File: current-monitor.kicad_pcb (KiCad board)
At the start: 2 copper layers, 50 x 50 mm, 60 parts, among them J1 SENSE, J2 BATTERY, J3 LCD5110, J4 UART, J5 SWD, J6 JTAG, Q1 MUN5314DW1, U1 AP2210K-3.3, U2 MKL03Z8VFK4, U3 MCP6V71U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

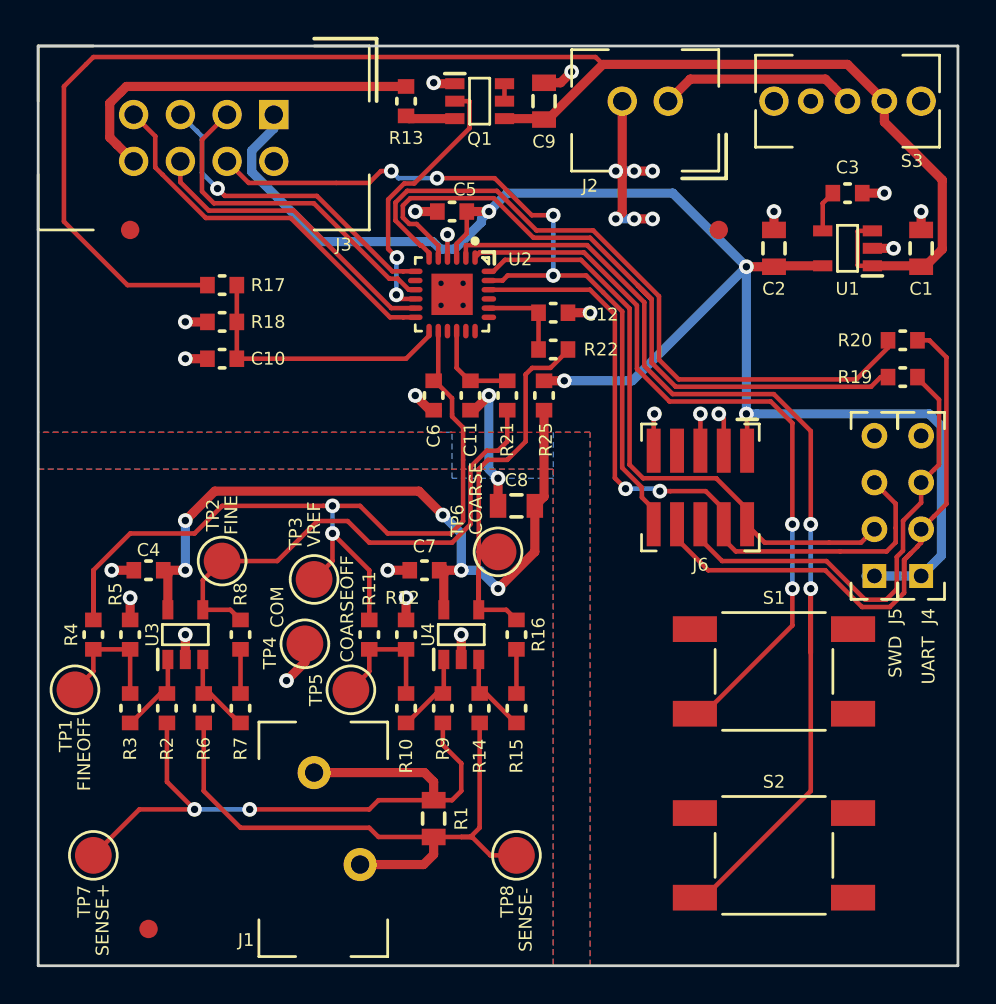
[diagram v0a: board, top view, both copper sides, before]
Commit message: improve power routing
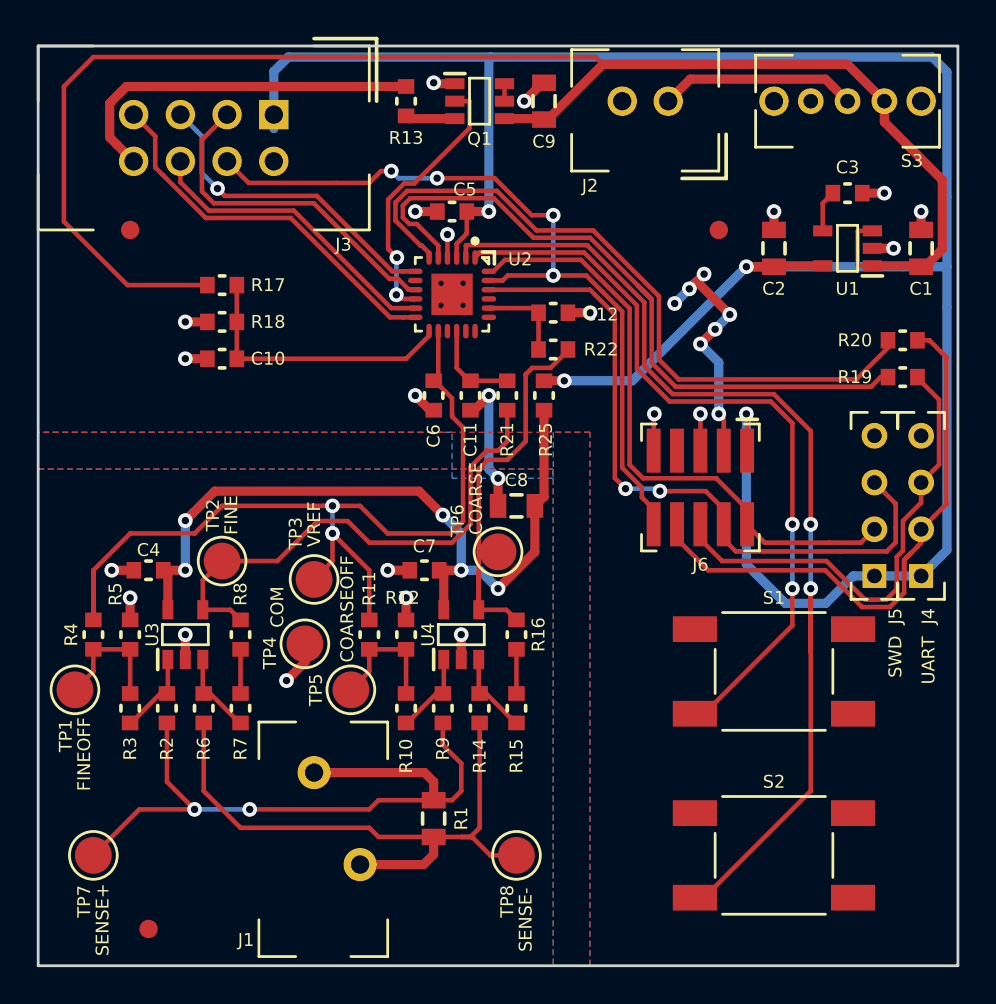
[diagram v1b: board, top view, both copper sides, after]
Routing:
- net +3V3: track 89.4 -> 131.0 mm
- net COM: track 49.6 -> 51.2 mm
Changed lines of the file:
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@@
     (thickness 1.6)
     (drawings 6)
-    (tracks 517)
+    (tracks 519)
     (zones 0)
     (modules 60)
@@
   (segment (start 125 112.8) (end 123 112.8) (width 0.25) (layer F.Cu) (net 3))
   (segment (start 125 112.8) (end 125 115.2) (width 0.25) (layer F.Cu) (net 3))
-  (segment (start 137.4 86.8) (end 138.4 86.8) (width 0.5) (layer F.Cu) (net 4))
-  (via (at 138.4 86.8) (size 0.8) (drill 0.4) (layers F.Cu B.Cu) (net 4))
-  (segment (start 136.4 86.8) (end 137.4 86.8) (width 0.5) (layer B.Cu) (net 4))
-  (via (at 137.4 86.8) (size 0.8) (drill 0.4) (layers F.Cu B.Cu) (net 4))
-  (segment (start 136.75 87) (end 136.6 87) (width 0.5) (layer F.Cu) (net 4))
-  (segment (start 136.6 87) (end 136.4 86.8) (width 0.5) (layer F.Cu) (net 4))
-  (via (at 136.4 86.8) (size 0.8) (drill 0.4) (layers F.Cu B.Cu) (net 4))
-  (segment (start 136.75 87) (end 136.75 89.05) (width 0.5) (layer F.Cu) (net 4))
-  (segment (start 136.75 83) (end 136.75 87) (width 0.5) (layer F.Cu) (net 4))
-  (segment (start 136.75 87) (end 136.75 86.8) (width 0.5) (layer F.Cu) (net 4))
-  (segment (start 137.4 89.4) (end 138.4 89.4) (width 0.5) (layer F.Cu) (net 4))
-  (via (at 138.4 89.4) (size 0.8) (drill 0.4) (layers F.Cu B.Cu) (net 4))
-  (segment (start 136.4 89.4) (end 137.4 89.4) (width 0.5) (layer B.Cu) (net 4))
-  (via (at 137.4 89.4) (size 0.8) (drill 0.4) (layers F.Cu B.Cu) (net 4))
-  (segment (start 136.75 89.05) (end 136.4 89.4) (width 0.5) (layer F.Cu) (net 4))
-  (via (at 136.4 89.4) (size 0.8) (drill 0.4) (layers F.Cu B.Cu) (net 4))
-  (segment (start 132.5 82) (end 133.4 82) (width 0.5) (layer F.Cu) (net 4))
-  (segment (start 133.4 82) (end 134 81.4) (width 0.5) (layer F.Cu) (net 4))
-  (via (at 134 81.4) (size 0.8) (drill 0.4) (layers F.Cu B.Cu) (net 4))
+  (segment (start 132.5 82) (end 132.425002 82) (width 0.5) (layer F.Cu) (net 4))
+  (segment (start 132.425002 82) (end 131.425002 83) (width 0.5) (layer F.Cu) (net 4))
+  (via (at 131.425002 83) (size 0.8) (drill 0.4) (layers F.Cu B.Cu) (net 4))
+  (segment (start 140.4 93.2) (end 141.2 92.4) (width 0.5) (layer F.Cu) (net 4))
+  (via (at 141.2 92.4) (size 0.8) (drill 0.4) (layers F.Cu B.Cu) (net 4))
+  (segment (start 140.8 92.8) (end 140.4 93.2) (width 0.5) (layer F.Cu) (net 4))
+  (segment (start 140.8 92.8) (end 140.4 93.2) (width 0.5) (layer B.Cu) (net 4))
+  (via (at 140.4 93.2) (size 0.8) (drill 0.4) (layers F.Cu B.Cu) (net 4))
+  (segment (start 142.6 94.6) (end 140.8 92.8) (width 0.5) (layer F.Cu) (net 4))
+  (segment (start 139.6 94) (end 140.8 92.8) (width 0.5) (layer B.Cu) (net 4))
+  (via (at 139.6 94) (size 0.8) (drill 0.4) (layers F.Cu B.Cu) (net 4))
+  (segment (start 141.8 95.4) (end 142.6 94.6) (width 0.5) (layer B.Cu) (net 4))
+  (via (at 142.6 94.6) (size 0.8) (drill 0.4) (layers F.Cu B.Cu) (net 4))
+  (segment (start 141 96.2) (end 141.8 95.4) (width 0.5) (layer F.Cu) (net 4))
+  (via (at 141.8 95.4) (size 0.8) (drill 0.4) (layers F.Cu B.Cu) (net 4))
+  (segment (start 142 100) (end 142 97.2) (width 0.5) (layer B.Cu) (net 4))
+  (segment (start 142 97.2) (end 141 96.2) (width 0.5) (layer B.Cu) (net 4))
+  (via (at 141 96.2) (size 0.8) (drill 0.4) (layers F.Cu B.Cu) (net 4))
   (segment (start 129.5 99) (end 129.5 103) (width 0.5) (layer B.Cu) (net 4))
   (segment (start 129.5 103) (end 130 103.5) (width 0.5) (layer B.Cu) (net 4))
@@
   (segment (start 130.95 116.8) (end 131 116.8) (width 0.25) (layer F.Cu) (net 20))
   (segment (start 129.35 115.2) (end 130.95 116.8) (width 0.25) (layer F.Cu) (net 20))
+  (segment (start 150.2 92) (end 152 92) (width 0.5) (layer B.Cu) (net 21))
+  (segment (start 154.4 88.2) (end 154.4 92) (width 0.5) (layer B.Cu) (net 21))
+  (segment (start 154.4 92) (end 154.4 94.2) (width 0.5) (layer B.Cu) (net 21))
+  (segment (start 152 92) (end 154.4 92) (width 0.5) (layer B.Cu) (net 21))
+  (segment (start 154.4 88.2) (end 154.4 81.4) (width 0.5) (layer B.Cu) (net 21))
+  (segment (start 154.4 94.2) (end 154.4 107.41) (width 0.5) (layer B.Cu) (net 21))
+  (segment (start 143.5 100) (end 143.5 108.184002) (width 0.5) (layer B.Cu) (net 21))
+  (segment (start 143.5 108.184002) (end 145.615999 110.300001) (width 0.5) (layer B.Cu) (net 21))
+  (segment (start 145.615999 110.300001) (end 147.819999 110.300001) (width 0.5) (layer B.Cu) (net 21))
+  (segment (start 147.819999 110.300001) (end 149.31 108.81) (width 0.5) (layer B.Cu) (net 21))
+  (segment (start 149.31 108.81) (end 150.46 108.81) (width 0.5) (layer B.Cu) (net 21))
+  (segment (start 154.4 107.41) (end 154.100001 107.709999) (width 0.5) (layer B.Cu) (net 21))
+  (segment (start 143.5 92) (end 150.2 92) (width 0.5) (layer B.Cu) (net 21))
+  (segment (start 153.6 80.6) (end 129.6 80.6) (width 0.5) (layer B.Cu) (net 21))
+  (segment (start 129.6 80.6) (end 118.6 80.6) (width 0.5) (layer B.Cu) (net 21))
+  (segment (start 129.5 89) (end 129.5 80.7) (width 0.5) (layer B.Cu) (net 21))
+  (segment (start 129.5 80.7) (end 129.6 80.6) (width 0.5) (layer B.Cu) (net 21))
+  (segment (start 154.4 81.4) (end 153.6 80.6) (width 0.5) (layer B.Cu) (net 21))
+  (segment (start 118.6 80.6) (end 117.81 81.39) (width 0.5) (layer B.Cu) (net 21))
+  (segment (start 117.81 81.39) (end 117.81 83.73) (width 0.5) (layer B.Cu) (net 21))
   (segment (start 117.81 83.73) (end 117.81 84.493998) (width 0.5) (layer B.Cu) (net 21))
-  (segment (start 117.81 84.493998) (end 116.609999 85.693999) (width 0.5) (layer B.Cu) (net 21))
-  (segment (start 116.609999 85.693999) (end 116.609999 86.846001) (width 0.5) (layer B.Cu) (net 21))
-  (segment (start 116.609999 86.846001) (end 120.397999 90.634001) (width 0.5) (layer B.Cu) (net 21))
-  (segment (start 126.449999 90.634001) (end 126.865999 91.050001) (width 0.5) (layer B.Cu) (net 21))
-  (segment (start 127.634001 91.050001) (end 129.100001 89.584001) (width 0.5) (layer B.Cu) (net 21))
-  (segment (start 120.397999 90.634001) (end 126.449999 90.634001) (width 0.5) (layer B.Cu) (net 21))
-  (segment (start 126.865999 91.050001) (end 127.634001 91.050001) (width 0.5) (layer B.Cu) (net 21))
-  (segment (start 129.100001 89.584001) (end 129.100001 89.399999) (width 0.5) (layer B.Cu) (net 21))
-  (segment (start 129.100001 89.399999) (end 129.5 89) (width 0.5) (layer B.Cu) (net 21))
-  (segment (start 139.5 88) (end 130.5 88) (width 0.5) (layer B.Cu) (net 21))
-  (segment (start 130.5 88) (end 129.5 89) (width 0.5) (layer B.Cu) (net 21))
-  (segment (start 143.5 92) (end 139.5 88) (width 0.5) (layer B.Cu) (net 21))
   (segment (start 133.6 98.2) (end 137.3 98.2) (width 0.5) (layer B.Cu) (net 21))
   (segment (start 137.3 98.2) (end 143.5 92) (width 0.5) (layer B.Cu) (net 21))
   (segment (start 132.5 98.2) (end 133.6 98.2) (width 0.5) (layer F.Cu) (net 21))
   (via (at 133.6 98.2) (size 0.8) (drill 0.4) (layers F.Cu B.Cu) (net 21))
-  (segment (start 143.5 92) (end 143.5 100) (width 0.5) (layer B.Cu) (net 21))
   (segment (start 153 108.81) (end 154.100001 107.709999) (width 0.5) (layer B.Cu) (net 21))
-  (segment (start 144.065685 100) (end 143.5 100) (width 0.5) (layer B.Cu) (net 21))
-  (segment (start 154.100001 107.709999) (end 154.100001 100.661999) (width 0.5) (layer B.Cu) (net 21))
-  (segment (start 153.438002 100) (end 144.065685 100) (width 0.5) (layer B.Cu) (net 21))
-  (segment (start 154.100001 100.661999) (end 153.438002 100) (width 0.5) (layer B.Cu) (net 21))
   (segment (start 150 108.81) (end 153 108.81) (width 0.5) (layer B.Cu) (net 21))
   (segment (start 143.54 102) (end 143.54 100.04) (width 0.25) (layer F.Cu) (net 21))

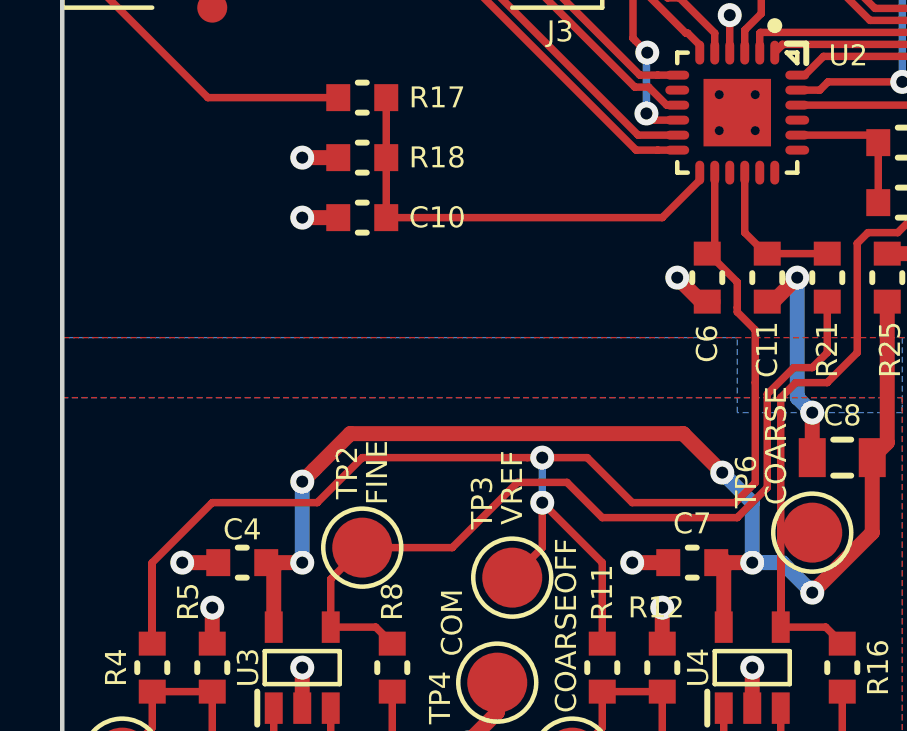
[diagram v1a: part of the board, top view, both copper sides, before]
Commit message: logo + silkscreen
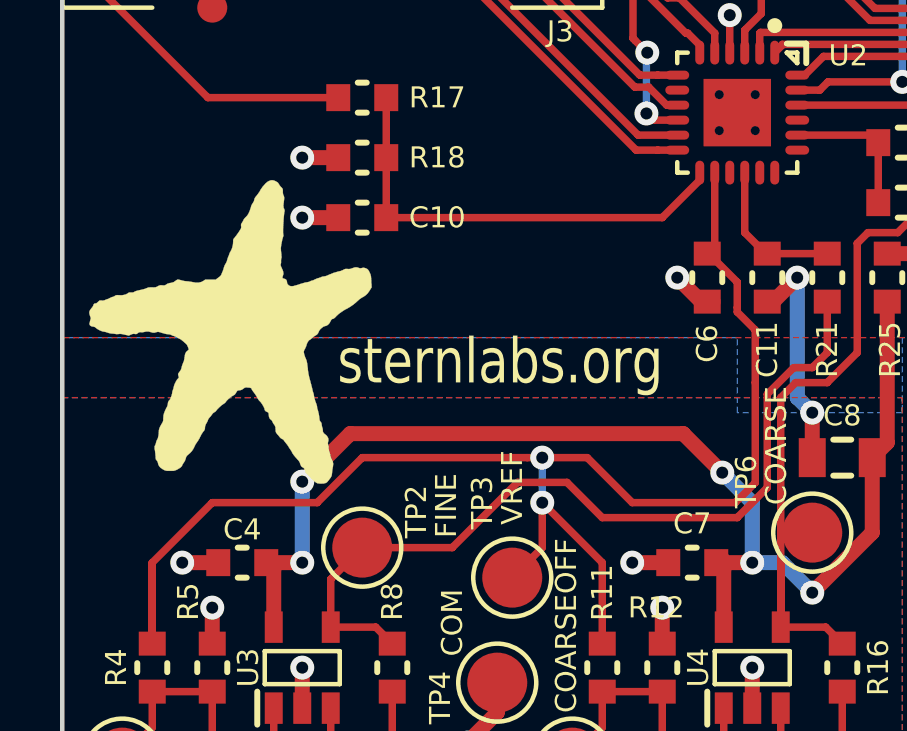
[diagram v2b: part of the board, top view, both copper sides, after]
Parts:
- added G***: LOGO, libs:starfish2-10, F.Cu at (110.6, 100.8)
- added G***: LOGO, libs:starfish2-10, B.Cu at (147.0, 120.0)
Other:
- board text added: "Current Monitor"
- board text added: "sternlabs.org"
- board text added: "v1.0 r0"
